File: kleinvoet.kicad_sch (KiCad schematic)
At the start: 37 parts, among them SW101 RESET, SW102 USER, U101 STM32F446RETx, Y101 12 MHz, Y102 32.768 kHz

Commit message: (sch) clean up items for BOM
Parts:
- D101, D102, D105: now fitted; now in the parts list
- R102, R103: now fitted
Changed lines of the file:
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@@
     (fill (type none))
+  )
+  (text_box "DO NOT POPULATE\n------------\nItems crossed out with a red 'X' are not to be populated. Some components are included as place holders, these are marked with the \"PH/DNP\" values."
+    (at 236.22 141.605 0) (size 40.005 15.24)
+    (stroke (width 0) (type default))
+    (fill (type none))
+    (effects (font (size 1.27 1.27) (thickness 0.254) bold) (justify left top))
   )
   (text_box "NOTE: USR_BTN controls BOOT0\n--------------------\nWhen user button is pressed during startup, it pulls BOOT0 high. This triggers the bootloader to go into DFU mode, allowing for the firmware to be updated over USB. Solder bridged JP1 can be broken to disable this functionalitiy."
@@
   )
   (symbol (lib_id "Device:R_Small") (at 179.705 117.475 0) (unit 1)
-    (in_bom yes) (on_board yes) (dnp yes)
+    (in_bom yes) (on_board yes) (dnp no)
     (property "Reference" "R102" (at 181.2036 116.3066 0)
       (effects (font (size 1.27 1.27)) (justify left))
@@
   )
   (symbol (lib_id "Device:LED_Small") (at 179.705 122.555 90) (unit 1)
-    (in_bom no) (on_board yes) (dnp yes)
+    (in_bom yes) (on_board yes) (dnp no)
     (property "Reference" "D101" (at 181.483 121.3866 90)
       (effects (font (size 1.27 1.27)) (justify right))
@@
   )
   (symbol (lib_id "Device:R_Small") (at 193.675 118.11 0) (unit 1)
-    (in_bom yes) (on_board yes) (dnp yes)
+    (in_bom yes) (on_board yes) (dnp no)
     (property "Reference" "R103" (at 195.1736 116.9416 0)
       (effects (font (size 1.27 1.27)) (justify left))
@@
   )
   (symbol (lib_id "Device:LED_Small") (at 193.675 123.19 90) (unit 1)
-    (in_bom no) (on_board yes) (dnp yes)
+    (in_bom yes) (on_board yes) (dnp no)
     (property "Reference" "D102" (at 195.453 122.0216 90)
       (effects (font (size 1.27 1.27)) (justify right))
@@
   )
   (symbol (lib_id "LED:SK6805") (at 205.74 150.495 0) (unit 1)
-    (in_bom no) (on_board yes) (dnp yes)
+    (in_bom yes) (on_board yes) (dnp no)
     (property "Reference" "D105" (at 215.9 147.3709 0)
       (effects (font (size 1.27 1.27)))

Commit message: (sch) exclude mounting holes & JP from BOM
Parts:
- JP101: now left out of the parts list
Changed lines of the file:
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@@
   )
   (symbol (lib_id "Jumper:SolderJumper_2_Bridged") (at 82.55 38.1 90) (unit 1)
-    (in_bom yes) (on_board yes) (dnp no) (fields_autoplaced)
+    (in_bom no) (on_board yes) (dnp no) (fields_autoplaced)
     (property "Reference" "JP101" (at 85.09 37.465 90)
       (effects (font (size 1.27 1.27)) (justify right))
@@
       (effects (font (size 1.27 1.27)) hide)
     )
+    (property "MPN" "" (at 82.55 38.1 0)
+      (effects (font (size 1.27 1.27)) hide)
+    )
+    (property "Mfr." "" (at 82.55 38.1 0)
+      (effects (font (size 1.27 1.27)) hide)
+    )

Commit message: (sch) fix BTN part number
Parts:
- SW101, SW102: MPN PTS636Sx25SMTRLFS -> PTS636 SM25 SMTR LFS
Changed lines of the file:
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@@
       (effects (font (size 1.27 1.27)) hide)
     )
-    (property "MPN" "PTS636Sx25SMTRLFS" (at 260.985 24.765 0)
+    (property "MPN" "PTS636 SM25 SMTR LFS" (at 260.985 24.765 0)
       (effects (font (size 1.27 1.27)) hide)
     )
@@
       (effects (font (size 1.27 1.27)) hide)
     )
-    (property "MPN" "PTS636Sx25SMTRLFS" (at 181.61 23.495 90)
-      (effects (font (size 1.27 1.27)) hide)
-    )
+    (property "MPN" "PTS636 SM25 SMTR LFS" (at 181.61 23.495 90)
+      (effects (font (size 1.27 1.27)) hide)
+    )

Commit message: (bom) add alt part number for neopixel
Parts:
- D105: MPN SK6805-2427 -> SK6805-2427 (ALT: 485-4492, 1528-2291-ND)
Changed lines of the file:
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@@
       (effects (font (size 1.27 1.27)) (justify left top) hide)
     )
-    (property "MPN" "SK6805-2427" (at 205.74 150.495 0)
+    (property "MPN" "SK6805-2427 (ALT: 485-4492, 1528-2291-ND)" (at 205.74 150.495 0)
       (effects (font (size 1.27 1.27)) hide)
     )

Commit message: chore(pinout): update IOC
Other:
- note removed: "TODO: UPDATE IOC"
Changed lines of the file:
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@@
-    (fill (type none))
-  )
-  (rectangle (start 82.55 57.15) (end 94.615 73.025)
-    (stroke (width 0) (type default))
     (fill (type none))
   )
@@
     (effects (font (size 1.27 1.27) (thickness 0.254) bold) (justify left bottom))
   )
-  (text "TODO: UPDATE IOC" (at 86.36 57.15 0)
-    (effects (font (size 1.27 1.27)) (justify left bottom))
-  )
   (text "ADC1_IN9" (at 138.43 82.55 0)

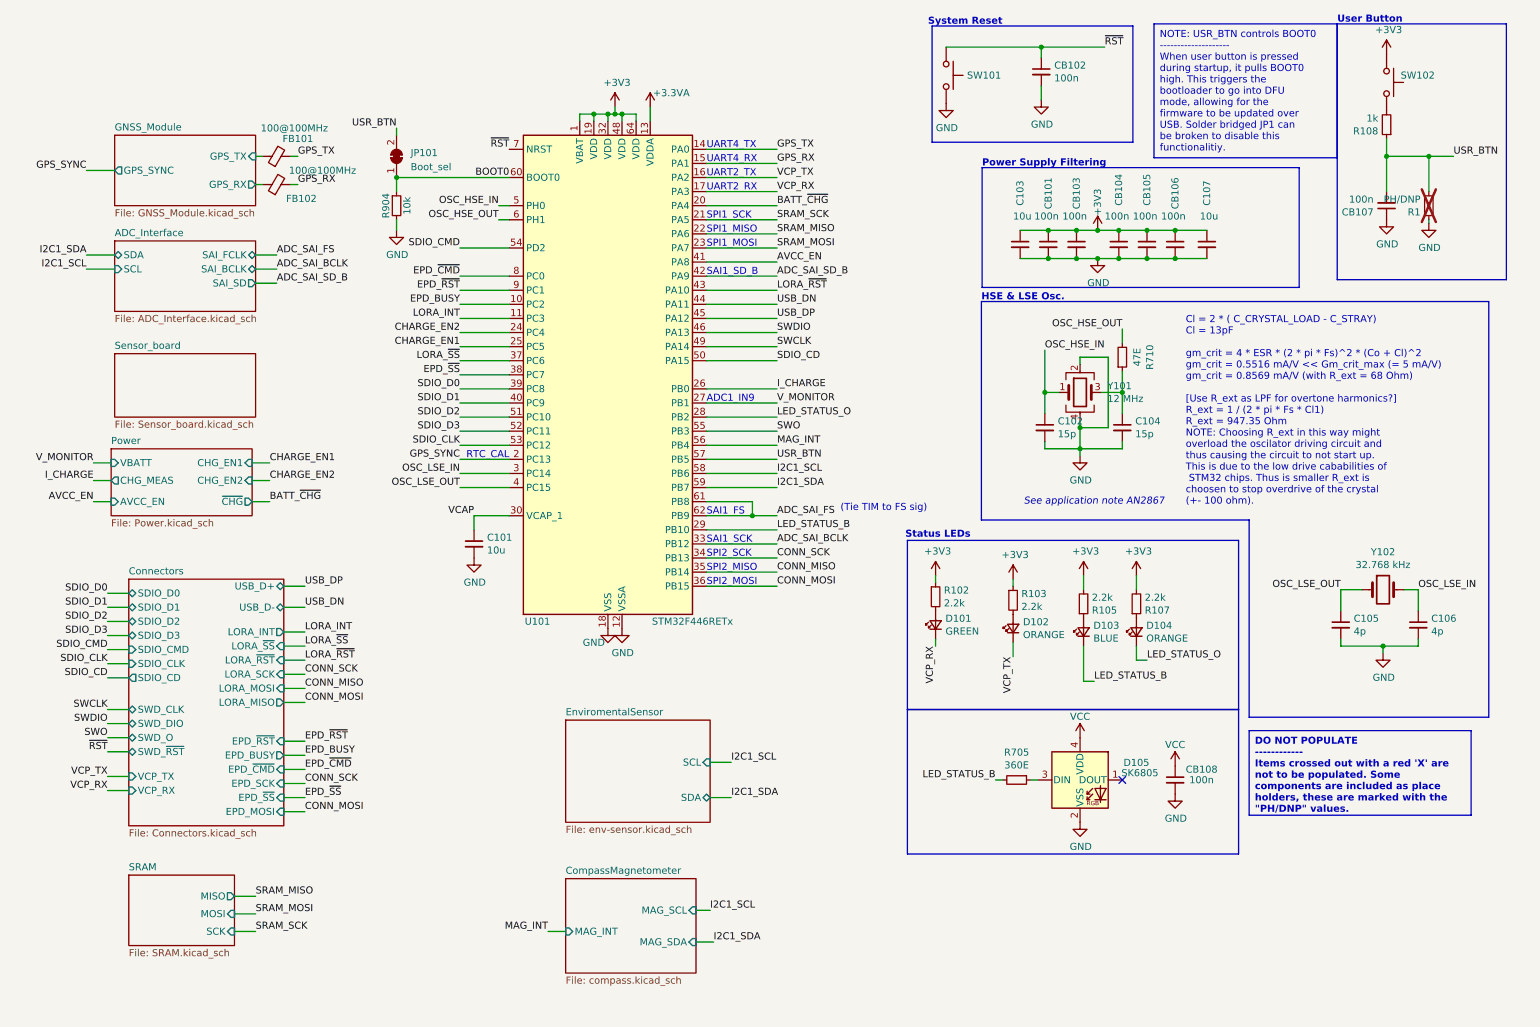
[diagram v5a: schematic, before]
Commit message: (pcb): fix boot selec & organise sch
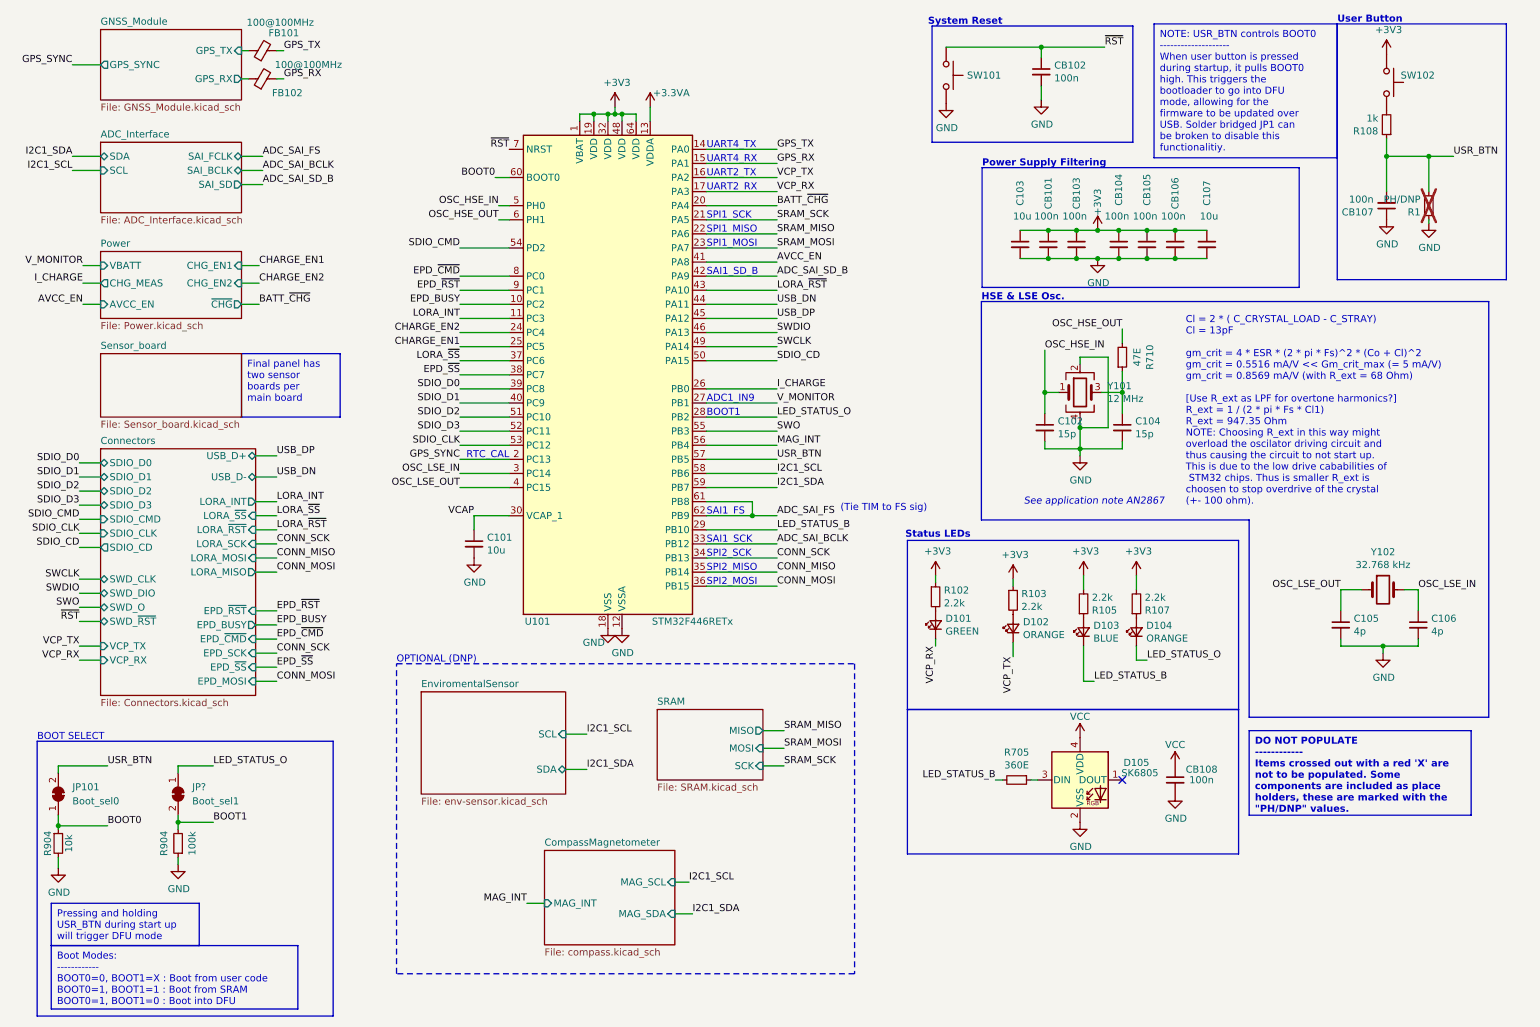
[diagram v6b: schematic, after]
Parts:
- added JP?: Boot_sel1, Jumper:SolderJumper-2_P1.3mm_Bridged_RoundedPad1.0x1.5mm, symbol Jumper:SolderJumper_2_Bridged
- added R904: 100k, Resistor_SMD:R_0402_1005Metric, symbol Device:R_Small
- JP101: value Boot_sel -> Boot_sel0
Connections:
- net GND: now also R904.1
- net LED_STATUS_O: now also JP?.1 (A)
- new net BOOT1: JP?.2 (B), R904.2
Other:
- note added: "BOOT SELECT"
- note added: "BOOT1"
- note added: "OPTIONAL (DNP)"
- moved on the sheet: FB101, FB102, JP101, R904

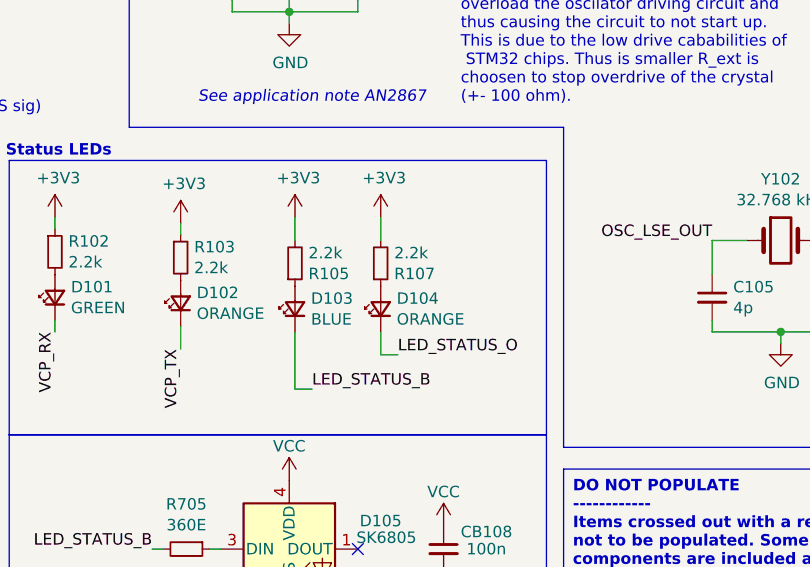
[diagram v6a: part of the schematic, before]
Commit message: bc(sch): change LEDs to push-pull
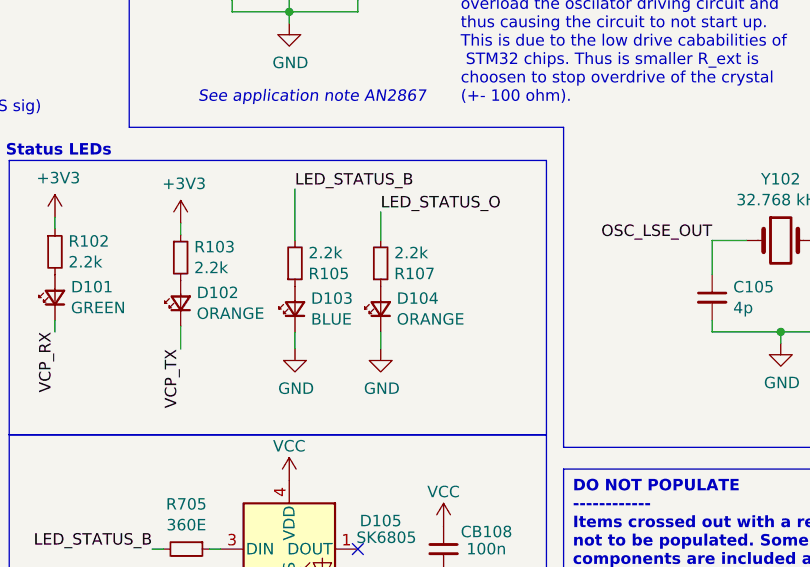
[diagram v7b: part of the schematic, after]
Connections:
- net +3V3: no longer R105.2, R107.2
- net GND: now also D103.1 (K), D104.1 (K)
- net LED_STATUS_B: now also R105.2; no longer D103.1 (K)
- net LED_STATUS_O: now also R107.2; no longer D104.1 (K)
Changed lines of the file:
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@@
+    (stroke (width 0) (type default))
+  )
+  (wire (pts (xy 215.9 126.365) (xy 215.9 128.27))
     (stroke (width 0) (type default))
   )
@@
     (stroke (width 0) (type default))
   )
-  (wire (pts (xy 206.375 126.365) (xy 206.375 132.715))
-    (stroke (width 0) (type default))
-  )
   (wire (pts (xy 93.98 77.47) (xy 102.87 77.47))
     (stroke (width 0) (type default))
@@
     (stroke (width 0) (type default))
   )
-  (wire (pts (xy 215.9 128.905) (xy 217.805 128.905))
-    (stroke (width 0) (type default))
-  )
   (wire (pts (xy 113.03 142.24) (xy 116.84 142.24))
     (stroke (width 0) (type default))
@@
     (stroke (width 0) (type default))
   )
+  (wire (pts (xy 206.375 110.49) (xy 206.375 116.205))
+    (stroke (width 0) (type default))
+  )
   (wire (pts (xy 102.87 59.69) (xy 93.98 59.69))
     (stroke (width 0) (type default))
@@
     (stroke (width 0) (type default))
   )
-  (wire (pts (xy 215.9 126.365) (xy 215.9 128.905))
-    (stroke (width 0) (type default))
-  )
   (wire (pts (xy 120.65 30.48) (xy 120.65 31.75))
     (stroke (width 0) (type default))
@@
     (stroke (width 0) (type default))
   )
-  (wire (pts (xy 215.9 113.665) (xy 215.9 116.205))
-    (stroke (width 0) (type default))
-  )
   (wire (pts (xy 208.915 51.435) (xy 205.105 51.435))
     (stroke (width 0) (type default))
@@
     (stroke (width 0) (type default))
   )
-  (wire (pts (xy 206.375 116.205) (xy 206.375 113.665))
-    (stroke (width 0) (type default))
-  )
   (wire (pts (xy 146.685 102.87) (xy 146.685 100.33))
     (stroke (width 0) (type default))
   )
+  (wire (pts (xy 215.9 113.03) (xy 215.9 116.205))
+    (stroke (width 0) (type default))
+  )
   (wire (pts (xy 29.21 98.425) (xy 25.4 98.425))
     (stroke (width 0) (type default))
@@
     (stroke (width 0) (type default))
   )
-  (wire (pts (xy 206.375 132.715) (xy 208.28 132.715))
-    (stroke (width 0) (type default))
-  )
   (wire (pts (xy 217.805 56.515) (xy 212.725 56.515))
     (stroke (width 0) (type default))
@@
   )
   (wire (pts (xy 128.27 29.21) (xy 128.27 31.75))
+    (stroke (width 0) (type default))
+  )
+  (wire (pts (xy 206.375 126.365) (xy 206.375 128.27))
     (stroke (width 0) (type default))
   )
@@
     (effects (font (size 1.27 1.27)) (justify right bottom))
   )
-  (label "LED_STATUS_B" (at 208.28 132.715 0) (fields_autoplaced)
-    (effects (font (size 1.27 1.27)) (justify left bottom))
-  )
-  (label "LED_STATUS_O" (at 217.805 128.905 0) (fields_autoplaced)
+  (label "LED_STATUS_B" (at 206.375 110.49 0) (fields_autoplaced)
+    (effects (font (size 1.27 1.27)) (justify left bottom))
+  )
+  (label "LED_STATUS_O" (at 215.9 113.03 0) (fields_autoplaced)
     (effects (font (size 1.27 1.27)) (justify left bottom))
   )
@@
     )
   )
+  (symbol (lib_id "power:GND") (at 215.9 128.27 0) (unit 1)
+    (in_bom yes) (on_board yes) (dnp no)
+    (property "Reference" "#PWR017" (at 215.9 134.62 0)
+      (effects (font (size 1.27 1.27)) hide)
+    )
+    (property "Value" "GND" (at 216.027 132.6642 0)
+      (effects (font (size 1.27 1.27)))
+    )
+    (property "Footprint" "" (at 215.9 128.27 0)
+      (effects (font (size 1.27 1.27)) hide)
+    )
+    (property "Datasheet" "" (at 215.9 128.27 0)
+      (effects (font (size 1.27 1.27)) hide)
+    )
+    (pin "1")
+    (instances
+      (project "kleinvoet"
+        (path "/4185c36c-c66e-4dbd-be5d-841e551f4885"
+          (reference "#PWR017") (unit 1)
+        )
+      )
+    )
+  )
   (symbol (lib_id "power:GND") (at 123.19 123.19 0) (unit 1)
     (in_bom yes) (on_board yes) (dnp no)
@@
     )
   )
-  (symbol (lib_id "power:+3V3") (at 206.375 113.665 0) (unit 1)
-    (in_bom yes) (on_board yes) (dnp no)
-    (property "Reference" "#PWR0111" (at 206.375 117.475 0)
-      (effects (font (size 1.27 1.27)) hide)
-    )
-    (property "Value" "+3V3" (at 206.756 109.2708 0)
-      (effects (font (size 1.27 1.27)))
-    )
-    (property "Footprint" "" (at 206.375 113.665 0)
-      (effects (font (size 1.27 1.27)) hide)
-    )
-    (property "Datasheet" "" (at 206.375 113.665 0)
-      (effects (font (size 1.27 1.27)) hide)
-    )
-    (pin "1")
-    (instances
-      (project "kleinvoet"
-        (path "/4185c36c-c66e-4dbd-be5d-841e551f4885"
-          (reference "#PWR0111") (unit 1)
-        )
-      )
-    )
-  )
   (symbol (lib_id "Device:R_Small") (at 194.31 150.495 270) (unit 1)
     (in_bom yes) (on_board yes) (dnp no)
@@
         (path "/4185c36c-c66e-4dbd-be5d-841e551f4885"
           (reference "#PWR02") (unit 1)
+        )
+      )
+    )
+  )
+  (symbol (lib_id "power:GND") (at 206.375 128.27 0) (unit 1)
+    (in_bom yes) (on_board yes) (dnp no)
+    (property "Reference" "#PWR016" (at 206.375 134.62 0)
+      (effects (font (size 1.27 1.27)) hide)
+    )
+    (property "Value" "GND" (at 206.502 132.6642 0)
+      (effects (font (size 1.27 1.27)))
+    )
+    (property "Footprint" "" (at 206.375 128.27 0)
+      (effects (font (size 1.27 1.27)) hide)
+    )
+    (property "Datasheet" "" (at 206.375 128.27 0)
+      (effects (font (size 1.27 1.27)) hide)
+    )
+    (pin "1")
+    (instances
+      (project "kleinvoet"
+        (path "/4185c36c-c66e-4dbd-be5d-841e551f4885"
+          (reference "#PWR016") (unit 1)
         )
       )
@@
         )
       )
-    )
-  )
-  (symbol (lib_id "power:+3V3") (at 215.9 113.665 0) (unit 1)
-    (in_bom yes) (on_board yes) (dnp no)
-    (property "Reference" "#PWR0115" (at 215.9 117.475 0)
-      (effects (font (size 1.27 1.27)) hide)
-    )
-    (property "Value" "+3V3" (at 216.281 109.2708 0)
-      (effects (font (size 1.27 1.27)))
-    )
-    (property "Footprint" "" (at 215.9 113.665 0)
-      (effects (font (size 1.27 1.27)) hide)
-    )
-    (property "Datasheet" "" (at 215.9 113.665 0)
-      (effects (font (size 1.27 1.27)) hide)
-    )
-    (pin "1")
-    (instances
-      (project "kleinvoet"
-        (path "/4185c36c-c66e-4dbd-be5d-841e551f4885"
-          (reference "#PWR0115") (unit 1)
-        )
-      )
